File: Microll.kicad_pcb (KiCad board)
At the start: 2 copper layers, 35 x 43.2 mm, 30 parts, among them J1 Conn_01x08, J2 Conn_01x08, J3 Conn_01x08, J4 USB_C_Receptacle, J5 Conn_01x08, U1 ESP32-C3-WROOM-02-N4, U2 TLV76733DRVx, U3 STM32G0B1CBU6, U4 USBLC6-2P6, U5 DPDT_Switch_x2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

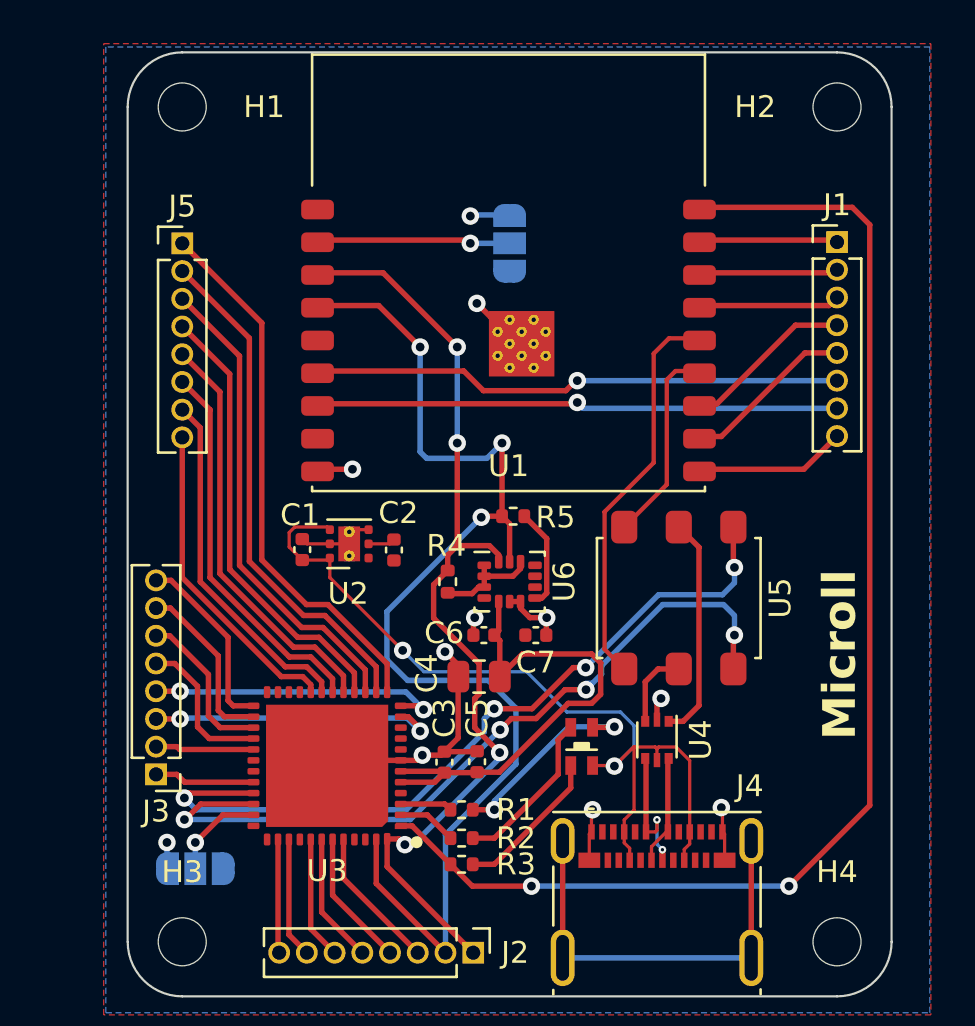
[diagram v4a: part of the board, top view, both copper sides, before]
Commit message: Added 3D model for USB-C. PCB finished!
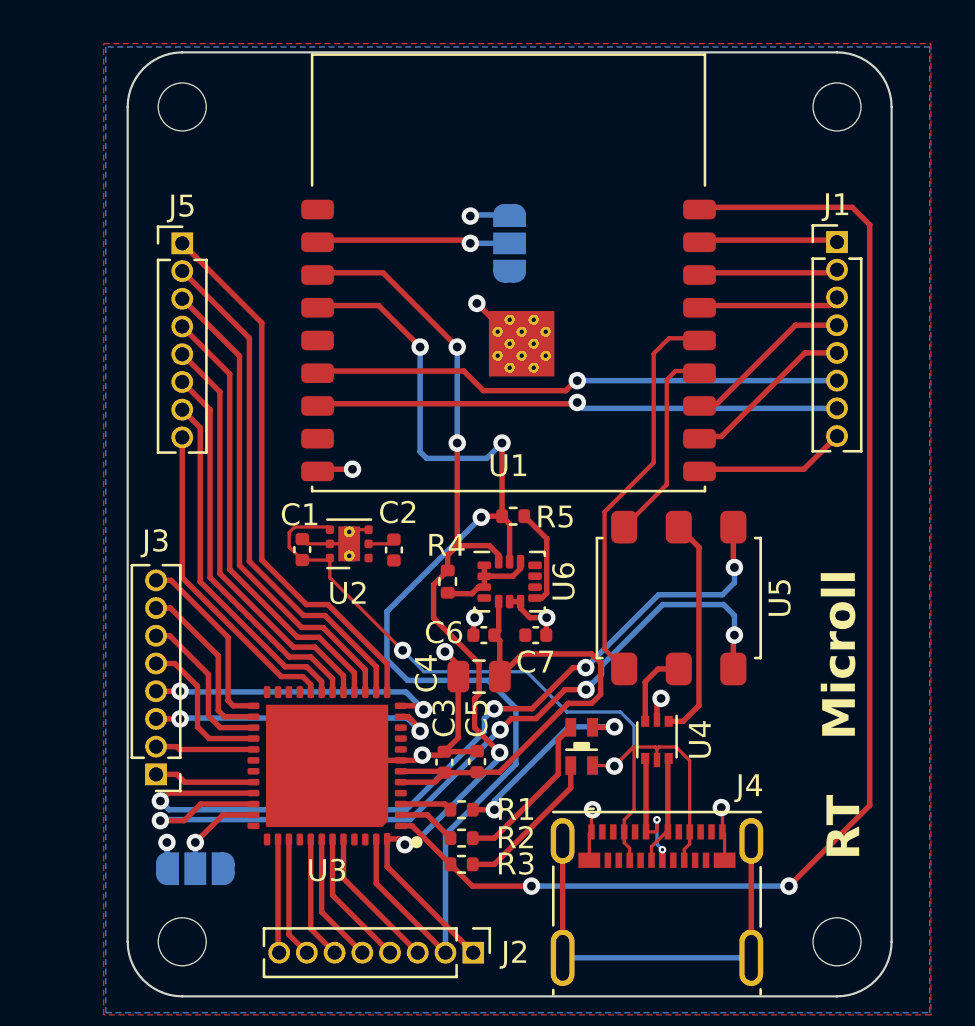
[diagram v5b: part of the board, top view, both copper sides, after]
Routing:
- net STM32_USB+: track 35.8 -> 38.1 mm
- net STM32_USB-: track 35.9 -> 38.1 mm
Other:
- board text added: "RT"

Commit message: PCB finished and ordered
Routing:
- net +3.3V: track 35.4 -> 36.9 mm
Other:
- board text added: "WayWayWay"
